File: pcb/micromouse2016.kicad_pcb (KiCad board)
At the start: 2 copper layers, 75.1 x 85.2 mm, 104 parts, among them IC1 RT7285/A, IC2 RT7285/A, IC3 REF1933, IC4 STM32F405RGTx, IC5 MPU6500, IC6 DRV8835, IC7 DRV8835, IC8 AD8604, IC9 NJM2746, P1 BATT1, P2 BATT2, P3 POWER_SW, P4 DEBUG_UART, P5 ARM_DEBUG, P6 MOTOR, P7 MOTOR, Q1 IRFML8244, Q2 IRFML8244, SW1 SW_PUSH, SW2 SW_PUSH

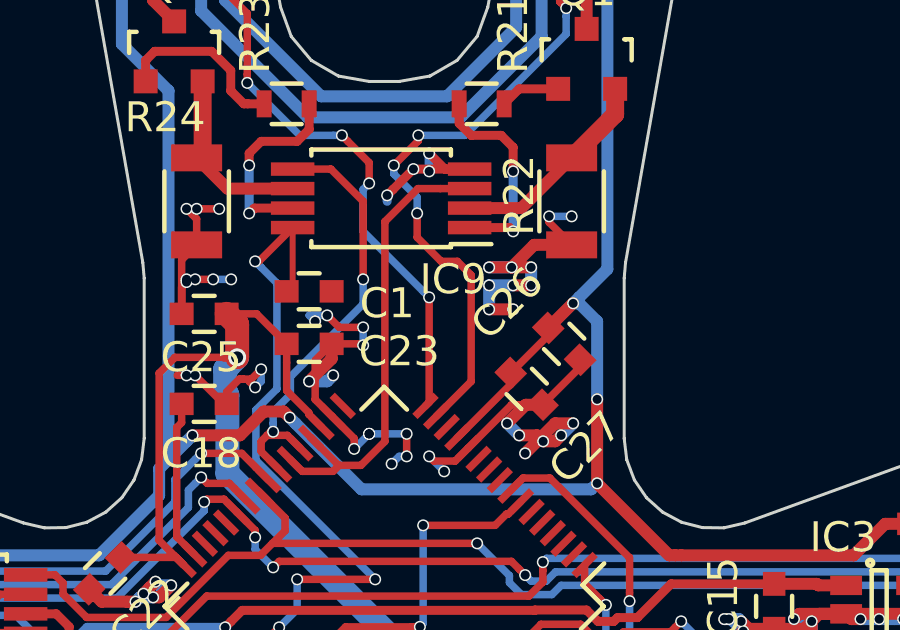
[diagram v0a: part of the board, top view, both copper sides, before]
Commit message: 実体配線図に抵抗を追加
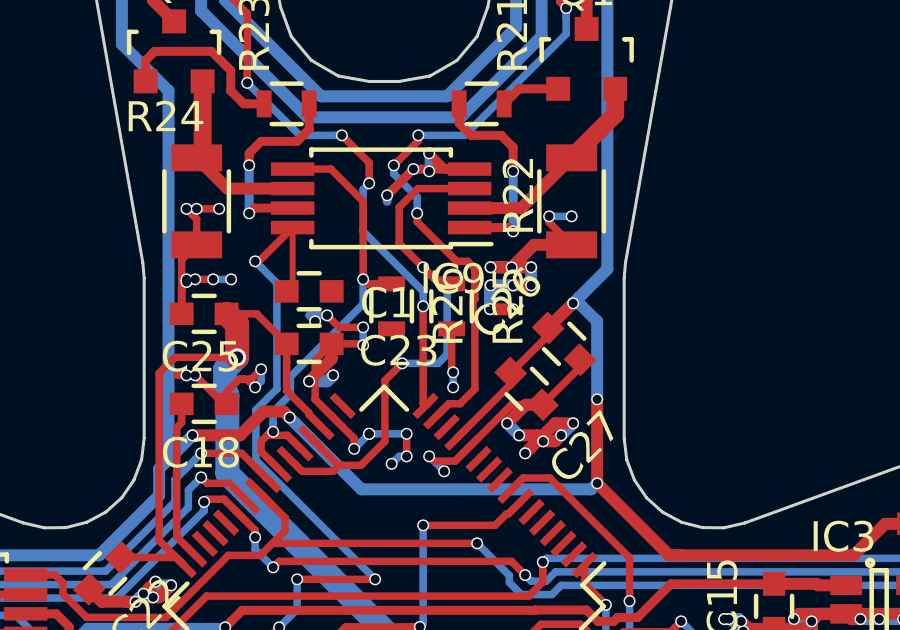
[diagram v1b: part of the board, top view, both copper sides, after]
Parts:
- added R25: 10k, Resistors_SMD:R_0603, F.Cu at (150.8, 53.5)
- added R26: 10k, Resistors_SMD:R_0603, F.Cu at (148.8, 53.5)
- R22, R24: value 33 1/4W -> 15 1/4W
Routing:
- net /ir_transmitter1/IN: track 15.7 -> 18.9 mm, vias 0 -> 2
- net GND: track 792.5 -> 794.3 mm, vias 588 -> 590
- net /ir_transmitter2/IN: track 14.7 -> 15.7 mm
